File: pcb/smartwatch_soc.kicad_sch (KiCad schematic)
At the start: 48 parts, among them J2 USB_B_Micro, Q1 PN2222A, Q2 PN2222A, Q3 BC338, Q4 BC338, SW1 SW_MEC_5G, SW2 Button, SW3 Button, SW4 Button, SW5 Button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

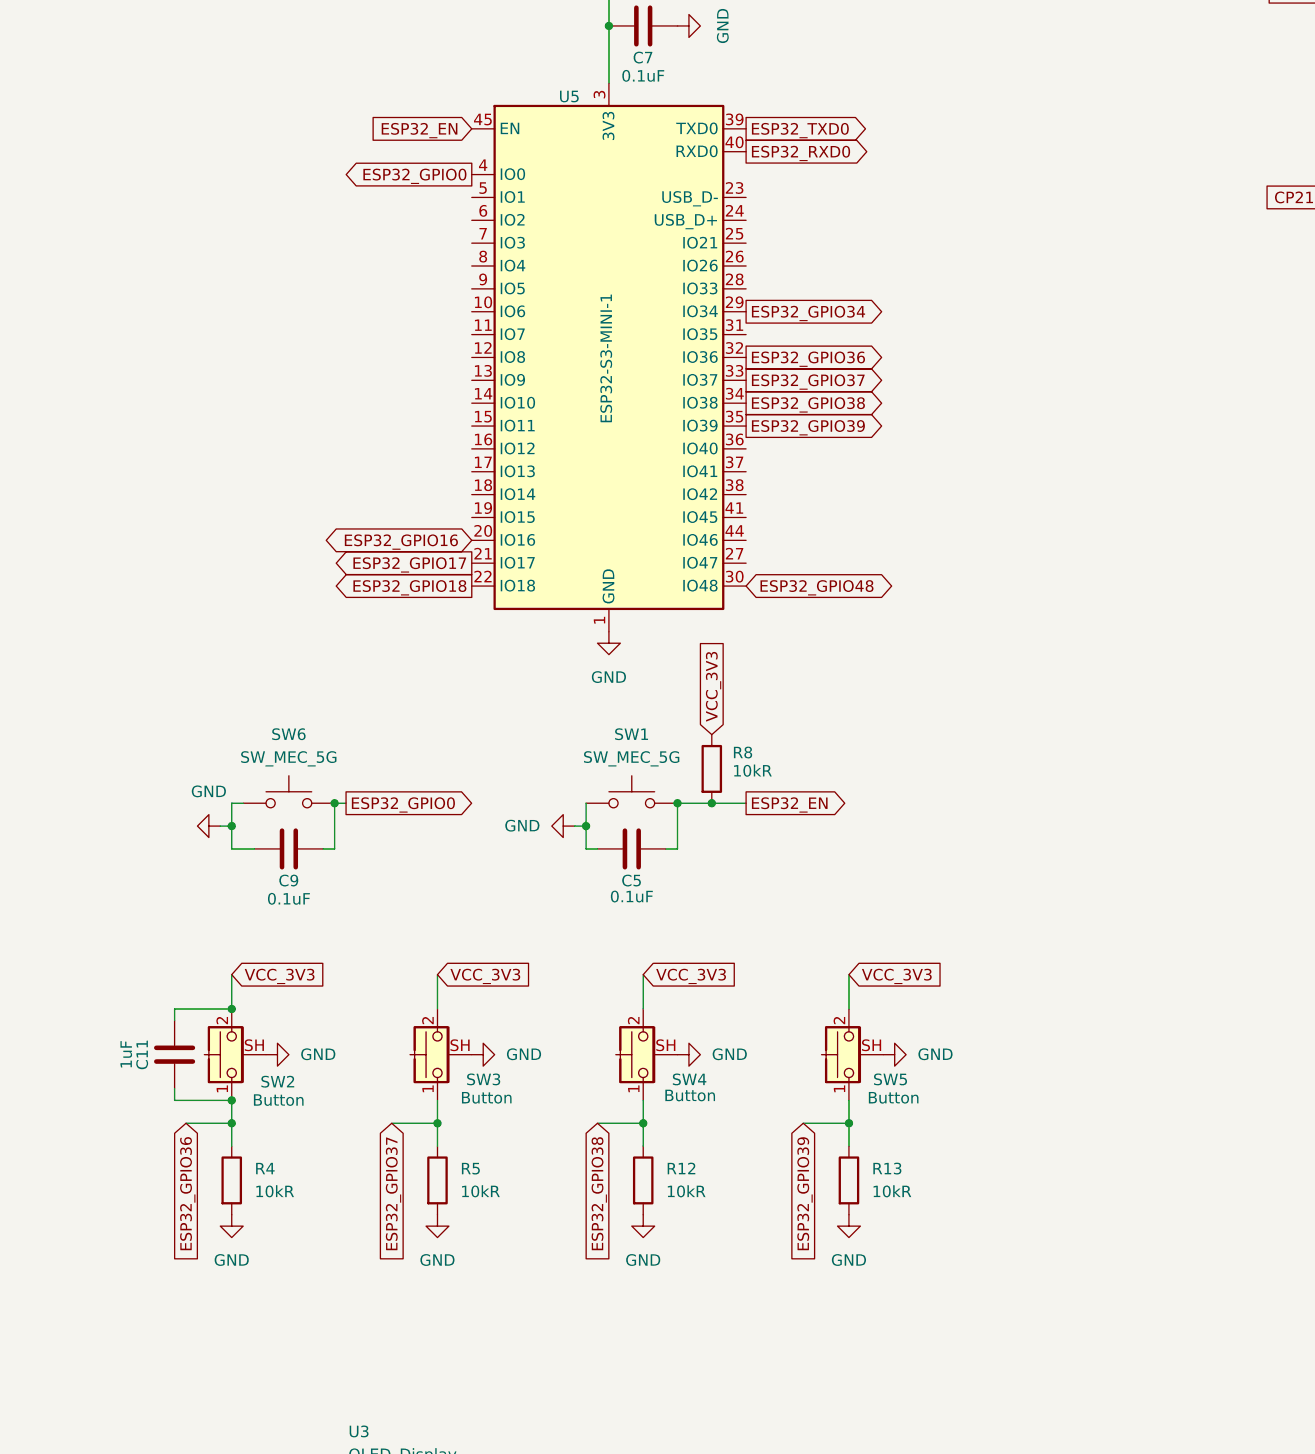
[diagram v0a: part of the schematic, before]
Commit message: updated en and gpio0 circuits
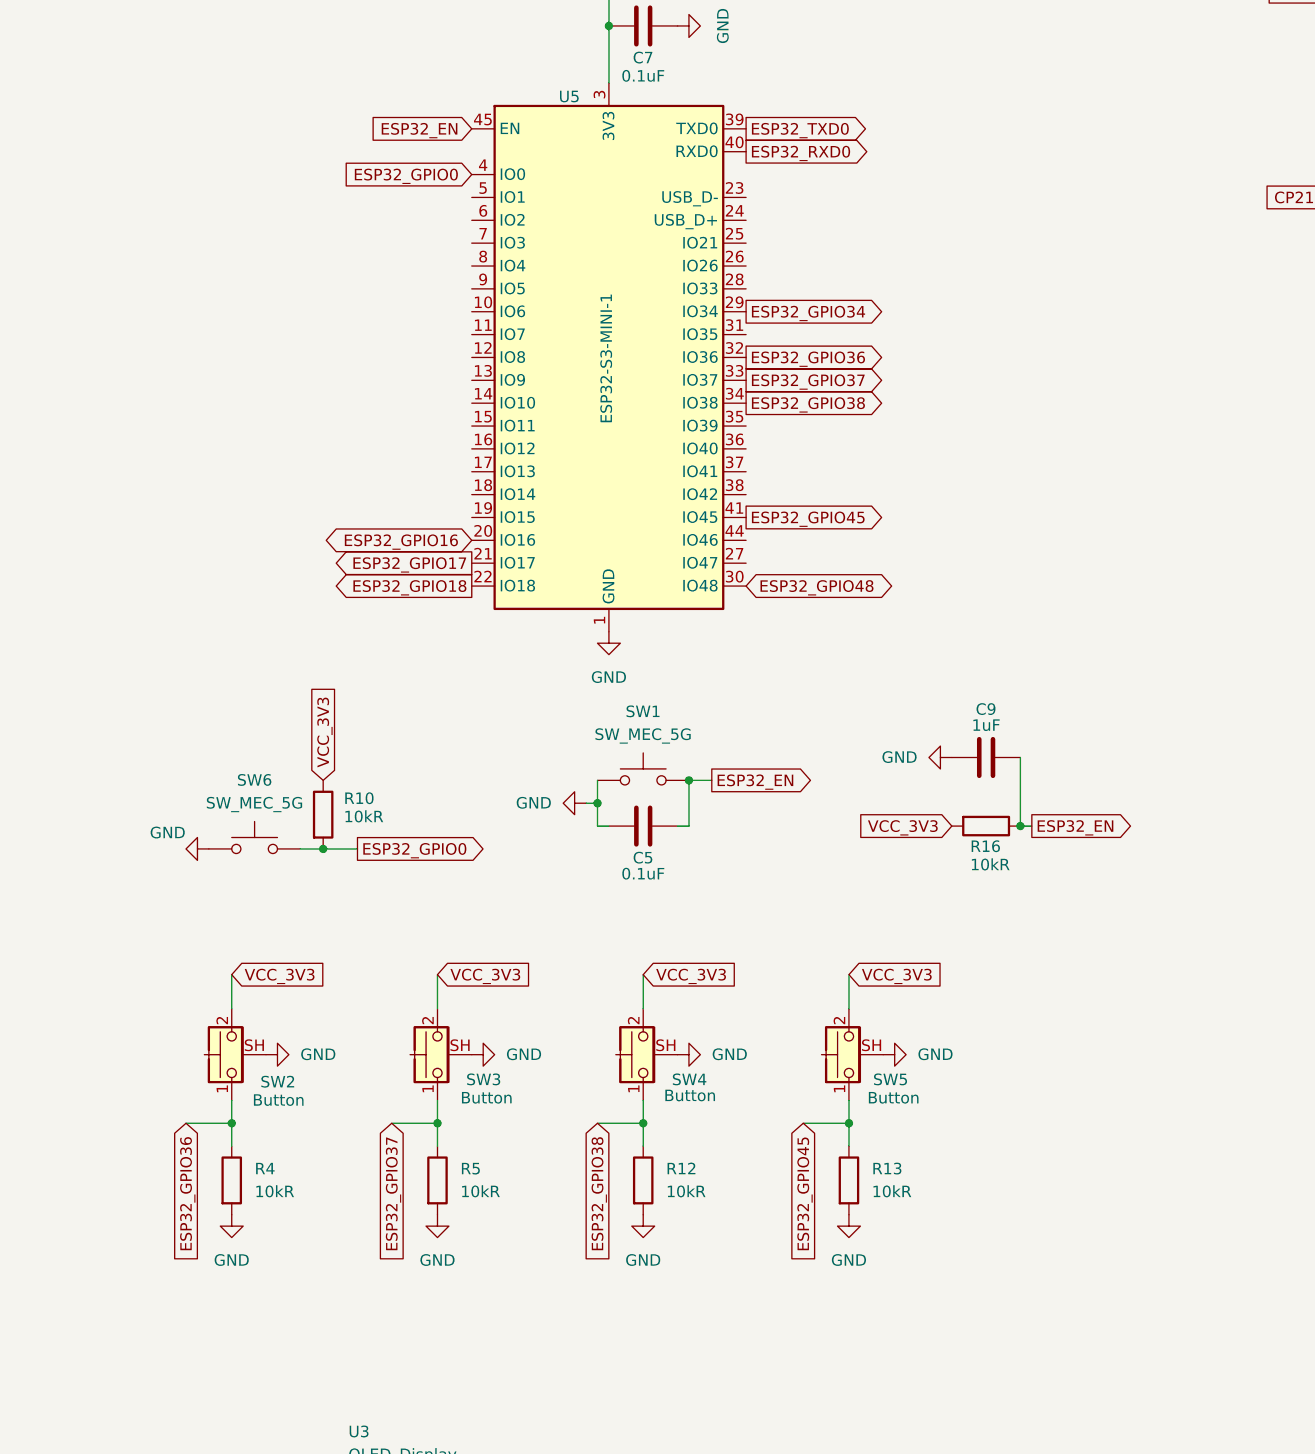
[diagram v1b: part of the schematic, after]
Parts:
- removed C11: 1uF, Capacitor_THT:C_Disc_D5.0mm_W2.5mm_P2.50mm, symbol Device:C
- removed R8: 10kR, Resistor_THT:R_Axial_DIN0204_L3.6mm_D1.6mm_P5.08mm_Horizontal, symbol Device:R
- added R10, R16: 10kR, Resistor_THT:R_Axial_DIN0204_L3.6mm_D1.6mm_P5.08mm_Horizontal, symbol Device:R
- C9: value 0.1uF -> 1uF
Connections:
- net ESP32_EN: now also C9.2, R16.1
- net ESP32_GPIO0: now also R10.2; no longer C9.2
- net VCC_3V3: now also R10.1, R16.2
- net ESP32_GPIO45: now reaches U5.41 (IO45)
- net ESP32_GPIO45: now also R13.1, SW5.1
- removed net ESP32_GPIO39: R13.1, SW5.1, U5.35 (IO39)
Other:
- moved on the sheet: C5, SW1, SW6

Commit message: started pcb layout
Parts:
- removed D3, D4: LED, LED_THT:LED_D2.0mm_W4.0mm_H2.8mm_FlatTop, symbol Device:LED
- removed Q1, Q2: PN2222A, Package_TO_SOT_THT:TO-92_Inline, symbol Transistor_BJT:PN2222A
- removed Q3, Q4: BC338, Package_TO_SOT_THT:TO-92_Inline, symbol Transistor_BJT:BC338
- removed R1: 22.1kR, Resistor_THT:R_Axial_DIN0204_L3.6mm_D1.6mm_P5.08mm_Horizontal, symbol Device:R
- removed R10, R3: 10kR, Resistor_THT:R_Axial_DIN0204_L3.6mm_D1.6mm_P5.08mm_Horizontal, symbol Device:R
- removed R11, R7: 310R, Resistor_THT:R_Axial_DIN0204_L3.6mm_D1.6mm_P5.08mm_Horizontal, symbol Device:R
- removed R14: 1kR, Resistor_THT:R_Axial_DIN0204_L3.6mm_D1.6mm_P5.08mm_Horizontal, symbol Device:R
- removed R15, R17, R6, R9: R, Resistor_THT:R_Axial_DIN0204_L3.6mm_D1.6mm_P5.08mm_Horizontal, symbol Device:R
- removed R2: 47.5kR, Resistor_THT:R_Axial_DIN0204_L3.6mm_D1.6mm_P5.08mm_Horizontal, symbol Device:R
- removed SW1, SW6: SW_MEC_5G, Button_Switch_THT:SW_PUSH-12mm, symbol Switch:SW_MEC_5G
- removed U4: CP2102N-Axx-xQFN28, Package_DFN_QFN:QFN-28-1EP_5x5mm_P0.5mm_EP3.35x3.35mm, symbol Interface_USB:CP2102N-Axx-xQFN28
- added SW1, SW7: CK_KMS2xxGP, Button_Switch_SMD:SW_SPST_CK_KMS2xxGP, symbol Switch:CK_KMS2xxGP
- added U1: MIC5219-3.3YM5, Package_TO_SOT_SMD:SOT-23-5, symbol Regulator_Linear:MIC5219-3.3YM5
- C3: value 4.7uF -> 470pF
- C4: value 0.1uF -> 2.2uF
- C8: value 1uF -> 0.1uF
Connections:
- net ESP32_EN: now also SW7.1
- net ESP32_GPIO0: now also C8.2, SW1.1
- net GND: now also C3.1, SW1.2, SW1.SH (B), SW7.2, SW7.SH (B), U1.2 (GND); no longer C3.2
- net USB_DN: now also U5.23 (USB_D-)
- net USB_DP: now also U5.24 (USB_D+)
- net VCC_3V3: now also U1.5 (OUT); no longer C3.1
- net VCC_5V: now also U1.1 (IN), U1.3 (EN)
- net ESP32_RXD0: no longer names the net of U5.40 (RXD0)
- net ESP32_TXD0: no longer names the net of U5.39 (TXD0)
- new net: C3.2, U1.4 (BP)
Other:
- moved on the sheet: C1, C2, C5, C6, C7, C9, D1, D10, D6, D8, D9, J2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

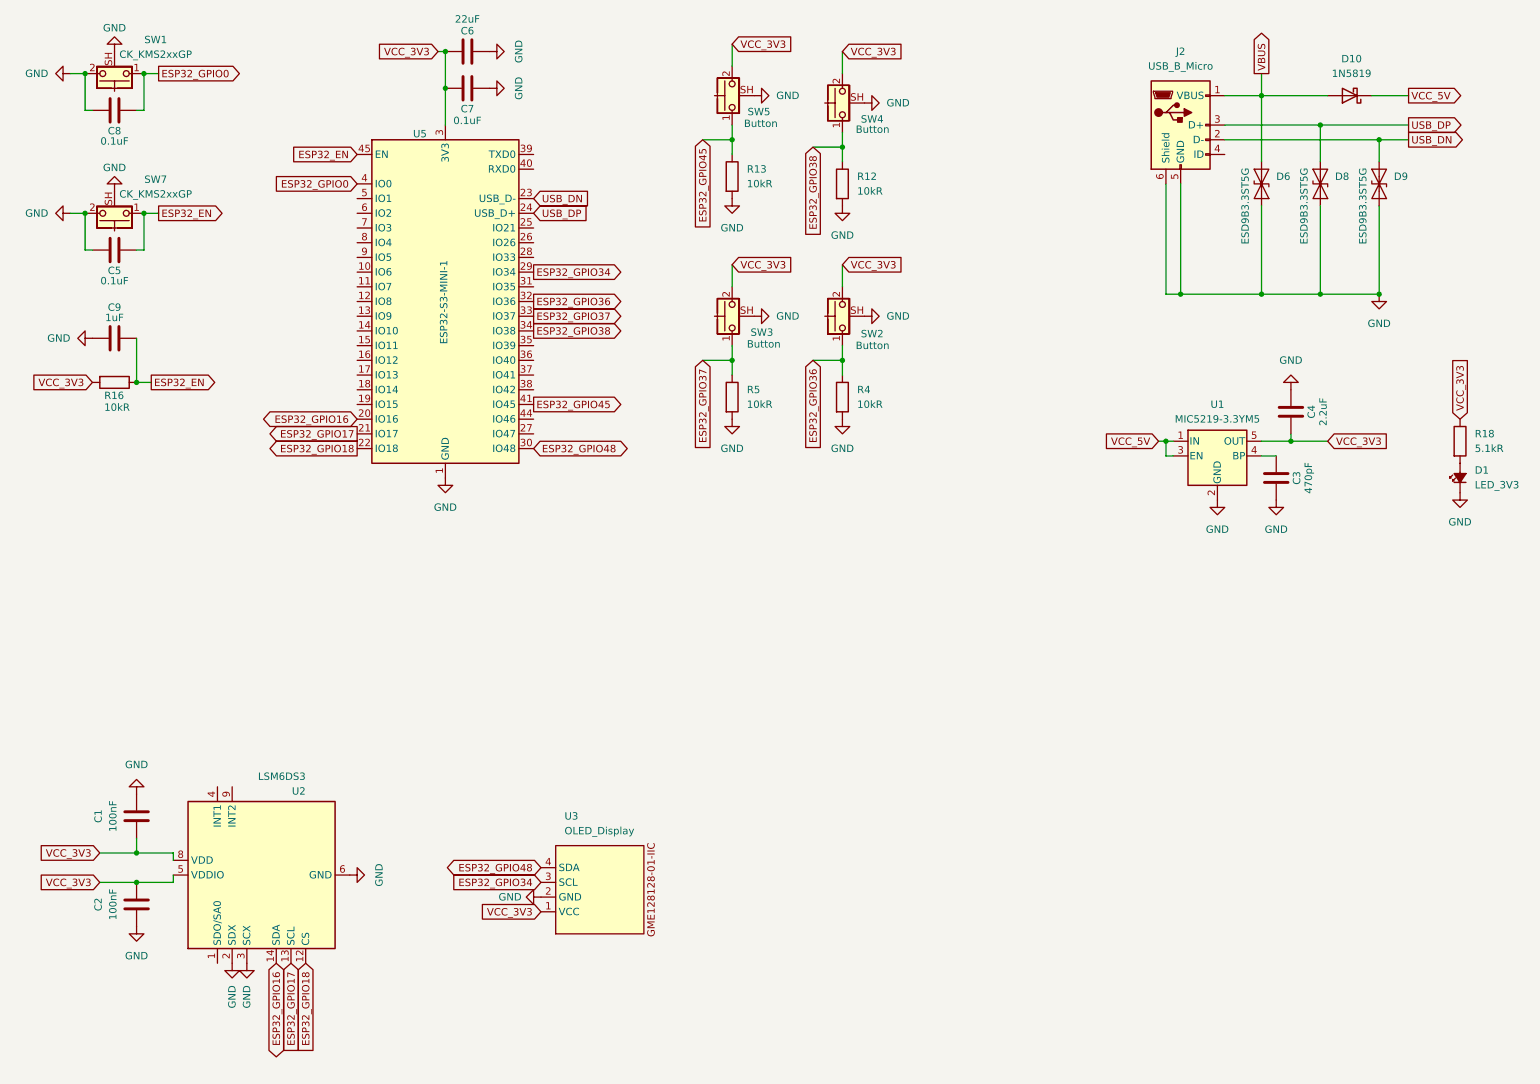
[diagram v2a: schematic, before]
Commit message: added labels
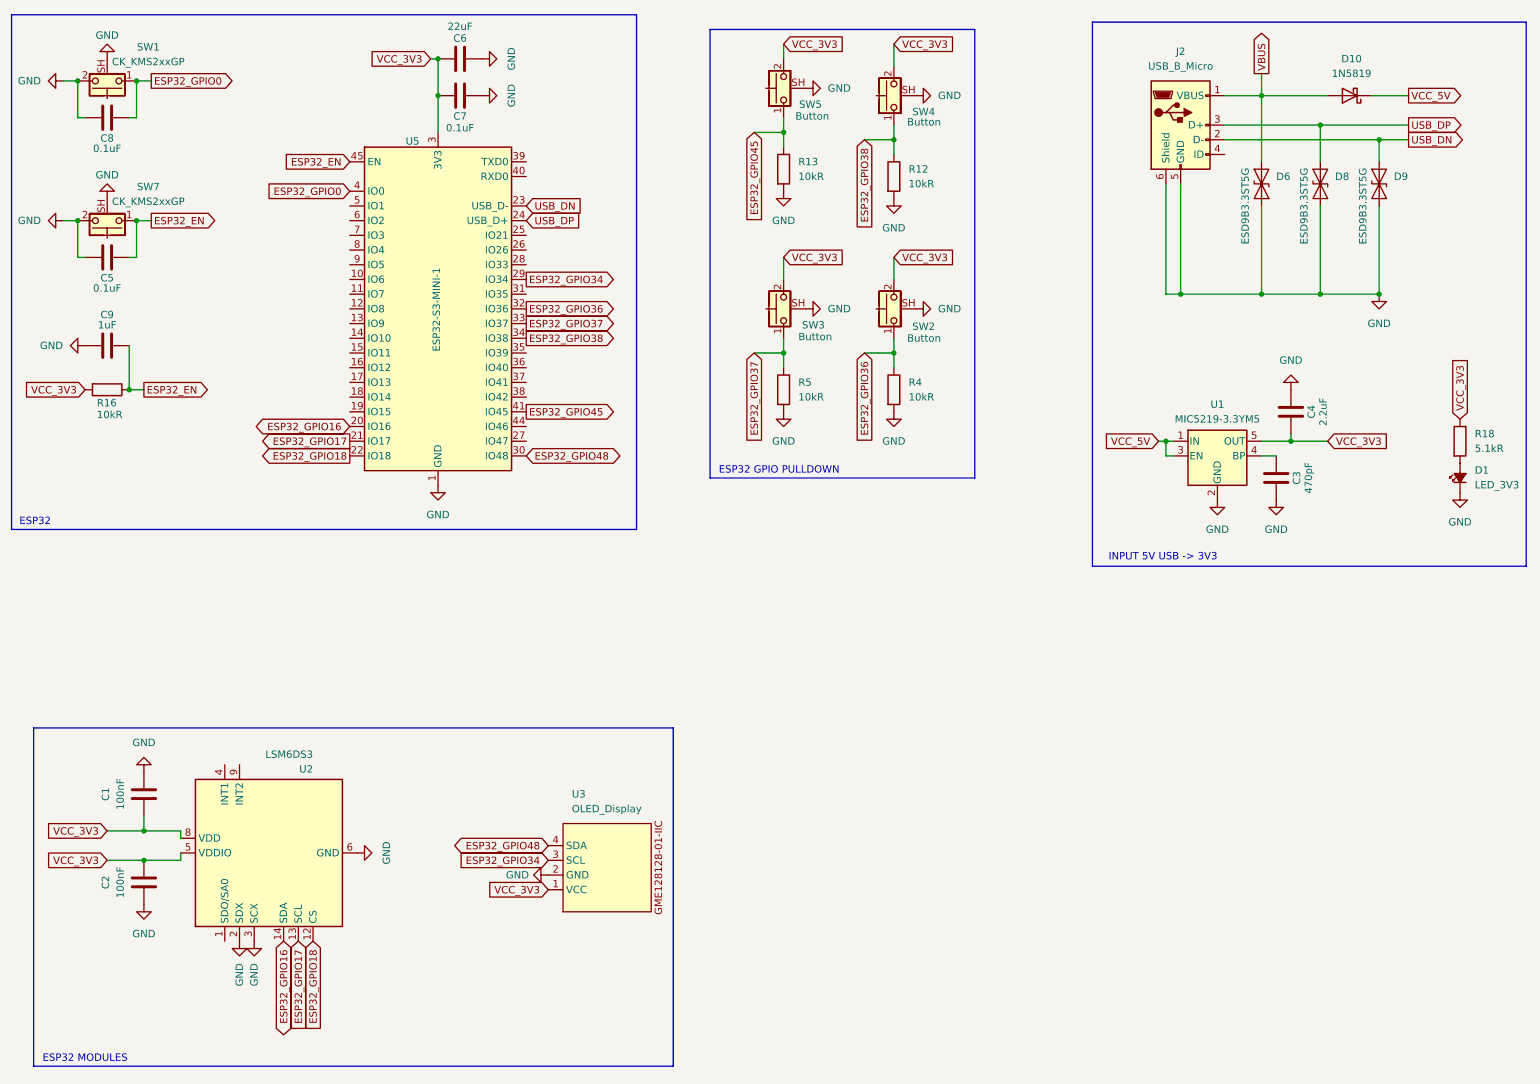
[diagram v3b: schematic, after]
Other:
- note added: "ESP32"
- note added: "ESP32 GPIO PULLDOWN"
- note added: "ESP32 MODULES"
- note added: "INPUT 5V USB -> 3V3"
- moved on the sheet: C1, C2, C5, C6, C7, C8, C9, R12, R13, R16, R4, R5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
